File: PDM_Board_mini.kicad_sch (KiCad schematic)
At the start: 17 parts, among them J1 705550003, J2 705550001, U1 FAN3852UC16X

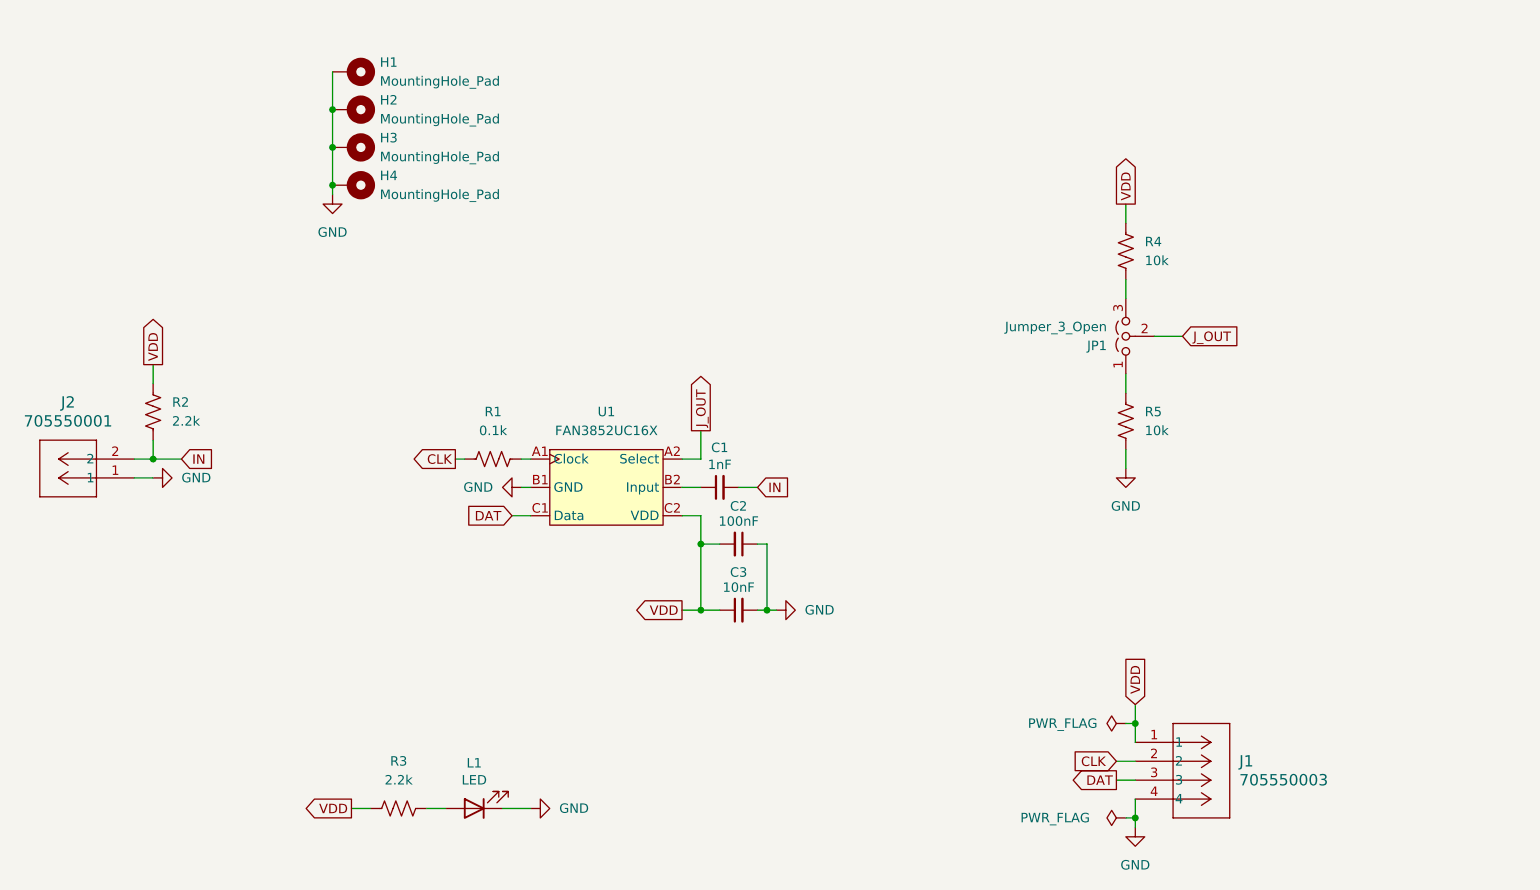
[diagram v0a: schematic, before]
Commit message: Updated PCB to 2 layer with components on only 1 side
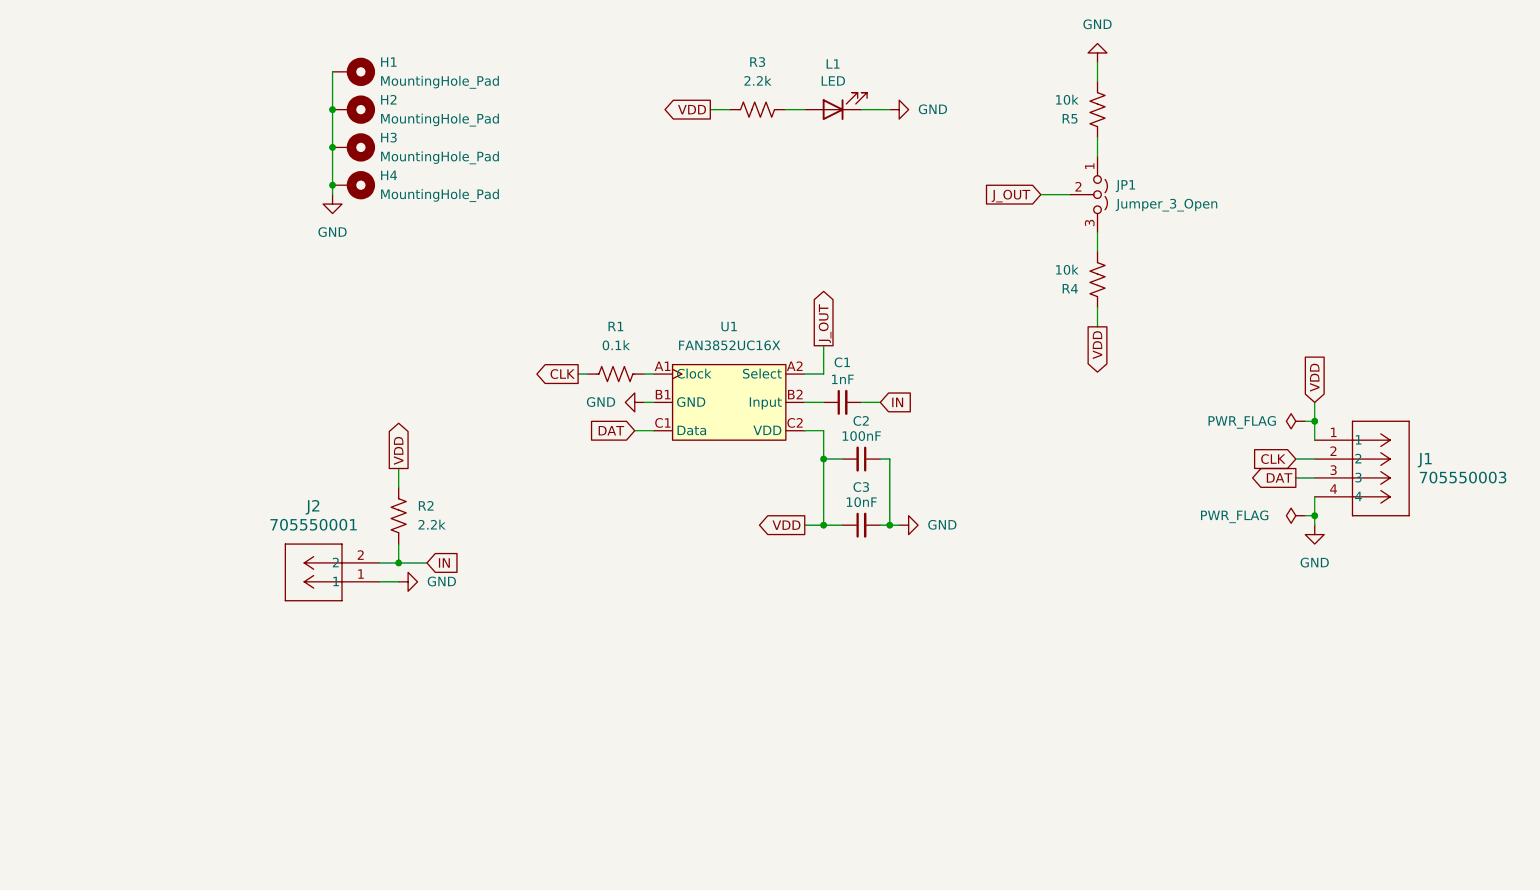
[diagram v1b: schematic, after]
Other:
- moved on the sheet: C1, C2, C3, J1, J2, JP1, L1, R1, R2, R3, R4, R5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
